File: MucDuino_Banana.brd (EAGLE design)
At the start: 91 x 46.6 mm, 40 parts, among them Q1 16 MHz, Q2 12 MHz, U1 ATMEGA328, X1 MINI-USB-UX60-MB-5ST

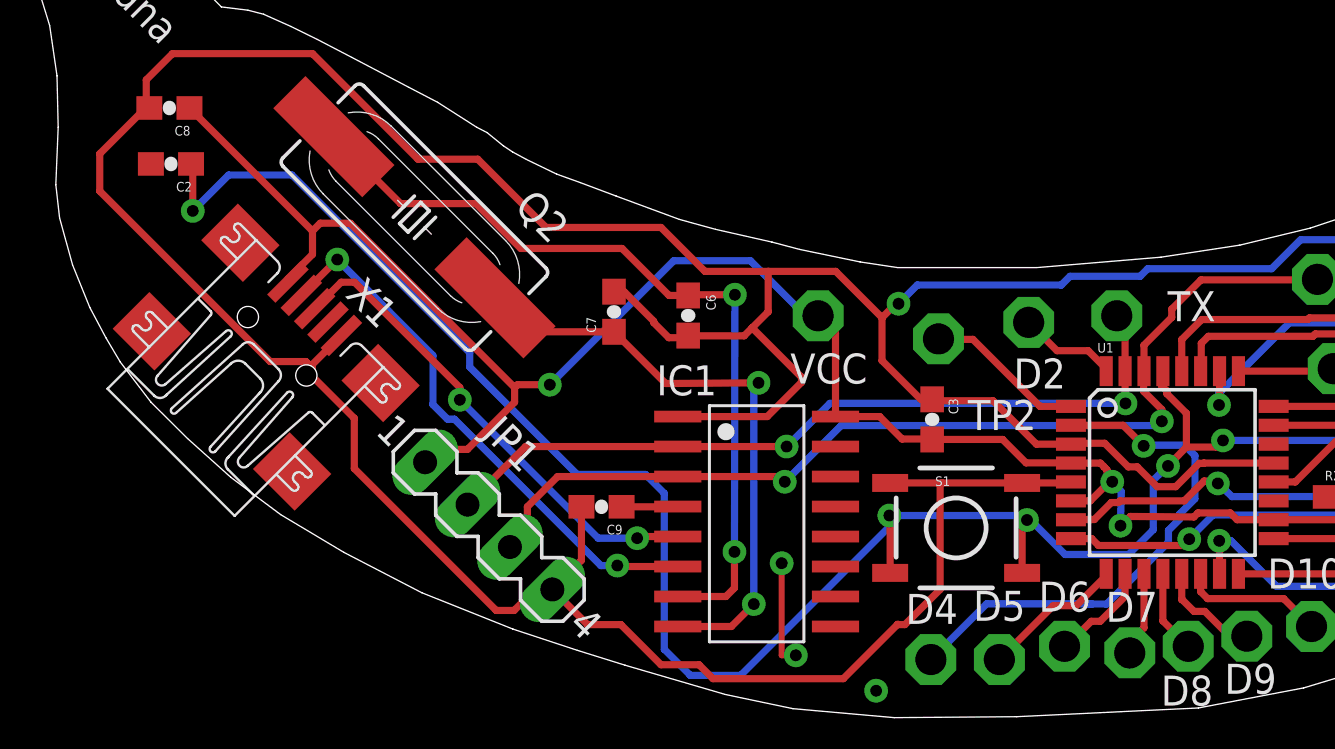
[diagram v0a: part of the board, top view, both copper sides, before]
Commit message: Ad Cherry variant of MucDuino, fix Banana Version, ad USB Uart Datascheet
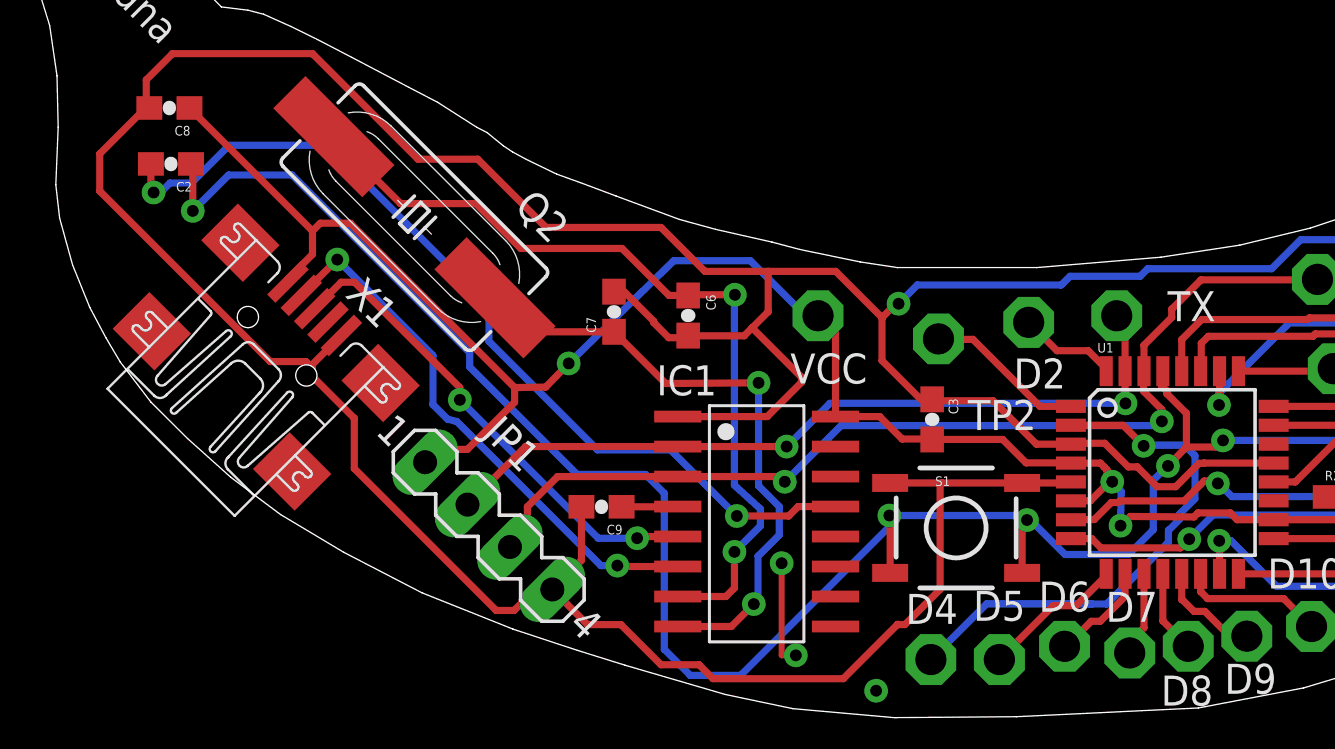
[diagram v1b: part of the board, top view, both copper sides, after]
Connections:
- net DTR: now also IC1.P$13
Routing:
- net DTR: track 0.00 -> 38.5 mm, vias 0 -> 2
- net N$5: track 35.1 -> 36.1 mm
- net N$6: track 25.8 -> 26.7 mm
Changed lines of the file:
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@@
 <wire x1="43.01" y1="21.88" x2="40.68" y2="24.21" width="0.3048" layer="16"/>
 <wire x1="40.68" y1="24.21" x2="37.43" y2="24.21" width="0.3048" layer="16"/>
-<wire x1="37.43" y1="24.21" x2="32.18" y2="18.96" width="0.3048" layer="16"/>
-<via x="32.18" y="18.96" extent="1-16" drill="0.5"/>
-<wire x1="32.18" y1="18.96" x2="30.81" y2="18.96" width="0.3048" layer="1"/>
-<wire x1="30.81" y1="18.96" x2="30.69" y2="18.84" width="0.3048" layer="1"/>
+<wire x1="37.43" y1="24.21" x2="32.98" y2="19.86" width="0.3048" layer="16"/>
+<via x="32.98" y="19.86" extent="1-16" drill="0.5"/>
+<wire x1="32.98" y1="19.86" x2="32.01" y2="18.86" width="0.3048" layer="1"/>
+<wire x1="32.01" y1="18.86" x2="30.69" y2="18.84" width="0.3048" layer="1"/>
 <wire x1="62.836096875" y1="13.241746875" x2="61.288253125" y2="13.241746875" width="0.3048" layer="1"/>
 <wire x1="61.288253125" y1="13.241746875" x2="61" y2="13.53" width="0.3048" layer="1"/>
@@
 <wire x1="84.58" y1="25.24" x2="85.295" y2="25.955" width="0.3048" layer="1"/>
 <wire x1="54.250896875" y1="12.441746875" x2="55.128253125" y2="12.441746875" width="0.3048" layer="1"/>
-<wire x1="55.128253125" y1="12.441746875" x2="55.42" y2="12.15" width="0.3048" layer="1"/>
-<wire x1="55.42" y1="12.15" x2="58.99" y2="12.15" width="0.3048" layer="1"/>
-<wire x1="58.99" y1="12.15" x2="59.26" y2="12.42" width="0.3048" layer="1"/>
+<wire x1="55.128253125" y1="12.441746875" x2="55.52" y2="12.05" width="0.3048" layer="1"/>
+<wire x1="55.52" y1="12.05" x2="58.89" y2="12.05" width="0.3048" layer="1"/>
+<wire x1="58.89" y1="12.05" x2="59.26" y2="12.42" width="0.3048" layer="1"/>
 <wire x1="59.41" y1="12.56" x2="59.41" y2="12.58" width="0.3048" layer="16"/>
 <wire x1="59.41" y1="12.58" x2="60.27" y2="13.44" width="0.3048" layer="16"/>
@@
 <signal name="DTR">
 <contactref element="C2" pad="2"/>
+<contactref element="IC1" pad="P$13"/>
+<wire x1="44.28" y1="13.8" x2="42.7" y2="13.8" width="0.3048" layer="1"/>
+<wire x1="42.7" y1="13.8" x2="42.3" y2="13.4" width="0.3048" layer="1"/>
+<wire x1="42.3" y1="13.4" x2="40.1" y2="13.4" width="0.3048" layer="1"/>
+<via x="40.1" y="13.4" extent="1-16" drill="0.5"/>
+<wire x1="40.1" y1="13.4" x2="37.3" y2="16.2" width="0.3048" layer="16"/>
+<wire x1="37.3" y1="16.2" x2="34.2" y2="16.2" width="0.3048" layer="16"/>
+<wire x1="34.2" y1="16.2" x2="29.6" y2="20.8" width="0.3048" layer="16"/>
+<wire x1="29.6" y1="20.8" x2="29.6" y2="22.3" width="0.3048" layer="16"/>
+<wire x1="29.6" y1="22.3" x2="22.8" y2="29.1" width="0.3048" layer="16"/>
+<wire x1="22.8" y1="29.1" x2="18.6" y2="29.1" width="0.3048" layer="16"/>
+<wire x1="18.6" y1="29.1" x2="17" y2="27.5" width="0.3048" layer="16"/>
+<wire x1="17" y1="27.5" x2="16.1" y2="27.5" width="0.3048" layer="16"/>
+<wire x1="16.1" y1="27.5" x2="15.7" y2="27.1" width="0.3048" layer="16"/>
+<wire x1="15.7" y1="27.1" x2="15.4" y2="27.1" width="0.3048" layer="16"/>
+<via x="15.4" y="27.1" extent="1-16" drill="0.5"/>
+<wire x1="15.4" y1="27.1" x2="15.2864" y2="27.2136" width="0.3048" layer="1"/>
+<wire x1="15.2864" y1="27.2136" x2="15.2864" y2="28.3088" width="0.3048" layer="1"/>
 </signal>
 <signal name="RXI">
@@
 <wire x1="40" y1="10.35" x2="40" y2="11.88" width="0.3048" layer="1"/>
 <via x="40" y="11.88" extent="1-16" drill="0.5"/>
-<wire x1="40" y1="11.88" x2="40.02" y2="22.77" width="0.3048" layer="16"/>
 <via x="40.02" y="22.77" extent="1-16" drill="0.5"/>
 <wire x1="40.02" y1="22.77" x2="38.22" y2="22.77" width="0.3048" layer="1"/>
 <wire x1="38.22" y1="22.77" x2="38.19" y2="22.74" width="0.3048" layer="1"/>
 <wire x1="38.19" y1="22.74" x2="38.04" y2="22.74" width="0.3048" layer="1"/>
+<wire x1="40" y1="11.88" x2="41.1" y2="12.98" width="0.3048" layer="16"/>
+<wire x1="41.1" y1="12.98" x2="41.1" y2="13.7" width="0.3048" layer="16"/>
+<wire x1="41.1" y1="13.7" x2="40" y2="14.7" width="0.3048" layer="16"/>
+<wire x1="40" y1="14.7" x2="40" y2="22.6" width="0.3048" layer="16"/>
+<wire x1="40" y1="22.6" x2="40.02" y2="22.62" width="0.3048" layer="16"/>
+<wire x1="40.02" y1="22.62" x2="40.02" y2="22.77" width="0.3048" layer="16"/>
 </signal>
 <signal name="N$6">
@@
 <wire x1="39.87" y1="8.72" x2="40.82" y2="9.67" width="0.3048" layer="1"/>
 <via x="40.82" y="9.67" extent="1-16" drill="0.5"/>
-<wire x1="40.82" y1="9.67" x2="40.82" y2="19.01" width="0.3048" layer="16"/>
 <wire x1="40.82" y1="19.01" x2="41.02" y2="19.04" width="0.3048" layer="16"/>
 <via x="41.02" y="19.04" extent="1-16" drill="0.5"/>
 <wire x1="41.02" y1="19.04" x2="37.09" y2="19.01" width="0.3048" layer="1"/>
 <wire x1="37.09" y1="19.01" x2="34.9" y2="21.2" width="0.3048" layer="1"/>
+<wire x1="40.82" y1="9.67" x2="41" y2="9.85" width="0.3048" layer="16"/>
+<wire x1="41" y1="9.85" x2="41" y2="11.7" width="0.3048" layer="16"/>
+<wire x1="41" y1="11.7" x2="41.9" y2="12.6" width="0.3048" layer="16"/>
+<wire x1="41.9" y1="12.6" x2="41.9" y2="13.8" width="0.3048" layer="16"/>
+<wire x1="41.9" y1="13.8" x2="41.02" y2="14.68" width="0.3048" layer="16"/>
+<wire x1="41.02" y1="14.68" x2="41.02" y2="19.04" width="0.3048" layer="16"/>
 </signal>
 <signal name="N$8">
@@
 <via x="35.04" y="11.3" extent="1-16" drill="0.5"/>
 <wire x1="35.04" y1="11.3" x2="34.34" y2="11.3" width="0.3048" layer="16"/>
-<wire x1="34.34" y1="11.3" x2="28.14" y2="17.5" width="0.3048" layer="16"/>
-<wire x1="28.14" y1="17.5" x2="27.85" y2="17.5" width="0.3048" layer="16"/>
+<wire x1="34.34" y1="11.3" x2="28.24" y2="17.4" width="0.3048" layer="16"/>
+<wire x1="28.24" y1="17.4" x2="27.85" y2="17.5" width="0.3048" layer="16"/>
 <wire x1="27.85" y1="17.5" x2="27.23" y2="18.12" width="0.3048" layer="16"/>
 <wire x1="27.23" y1="18.12" x2="27.23" y2="20.2" width="0.3048" layer="16"/>
